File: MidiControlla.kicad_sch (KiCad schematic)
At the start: 4 parts, among them U1 TCRT5000, U2 TCRT5000, U3 TCRT5000, U4 TCRT5000

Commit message: Add espressif c3
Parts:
- added U5: ESP32-S3-DevKitC, Espressif:ESP32-S3-DevKitC, symbol Espressif:ESP32-S3-DevKitC
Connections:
- new net: U5.1 (3V3), U5.2 (3V3)
- new net: U5.22 (GND), U5.23 (GND), U5.24 (GND), U5.44 (GND)
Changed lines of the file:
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@@
+    )
+  )
+  (symbol (lib_id "Espressif:ESP32-S3-DevKitC") (at 64.77 95.25 0) (unit 1)
+    (in_bom yes) (on_board yes) (dnp no) (fields_autoplaced)
+    (property "Reference" "U5" (at 66.9641 140.97 0)
+      (effects (font (size 1.27 1.27)) (justify left))
+    )
+    (property "Value" "ESP32-S3-DevKitC" (at 66.9641 143.51 0)
+      (effects (font (size 1.27 1.27)) (justify left))
+    )
+    (property "Footprint" "Espressif:ESP32-S3-DevKitC" (at 64.77 152.4 0)
+      (effects (font (size 1.27 1.27)) hide)
+    )
+    (property "Datasheet" "" (at 5.08 97.79 0)
+      (effects (font (size 1.27 1.27)) hide)
+    )
+    (pin "41")
+    (pin "19")
+    (pin "40")
+    (pin "39")
+    (pin "14")
+    (pin "34")
+    (pin "35")
+    (pin "37")
+    (pin "38")
+    (pin "36")
+    (pin "4")
+    (pin "5")
+    (pin "22")
+    (pin "24")
+    (pin "25")
+    (pin "8")
+    (pin "9")
+    (pin "6")
+    (pin "7")
+    (pin "30")
+    (pin "26")
+    (pin "27")
+    (pin "29")
+    (pin "3")
+    (pin "23")
+    (pin "28")
+    (pin "42")
+    (pin "2")
+    (pin "10")
+    (pin "13")
+    (pin "15")
+    (pin "18")
+    (pin "20")
+    (pin "1")
+    (pin "43")
+    (pin "11")
+    (pin "12")
+    (pin "17")
+    (pin "44")
+    (pin "21")
+    (pin "16")
+    (pin "33")
+    (pin "32")
+    (pin "31")
+    (instances
+      (project "MidiControlla"
+        (path "/6c0d32a8-1440-498c-b764-68a3bc199eca"
+          (reference "U5") (unit 1)
+        )
+      )
     )
   )

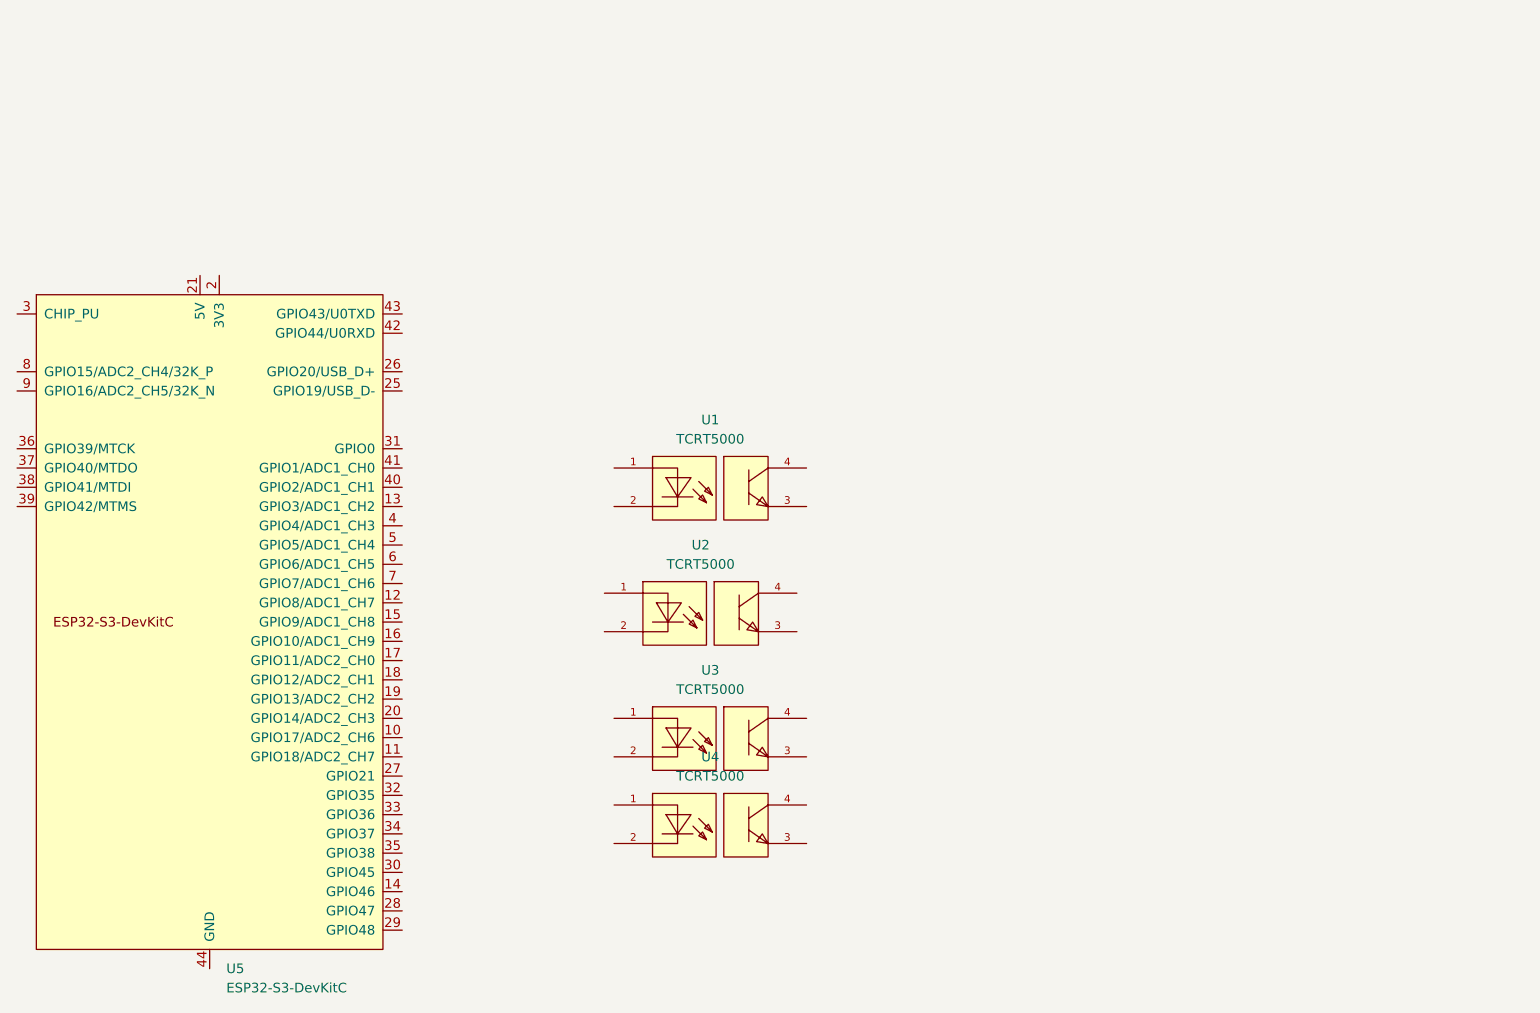
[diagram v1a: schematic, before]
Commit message: Add footprints
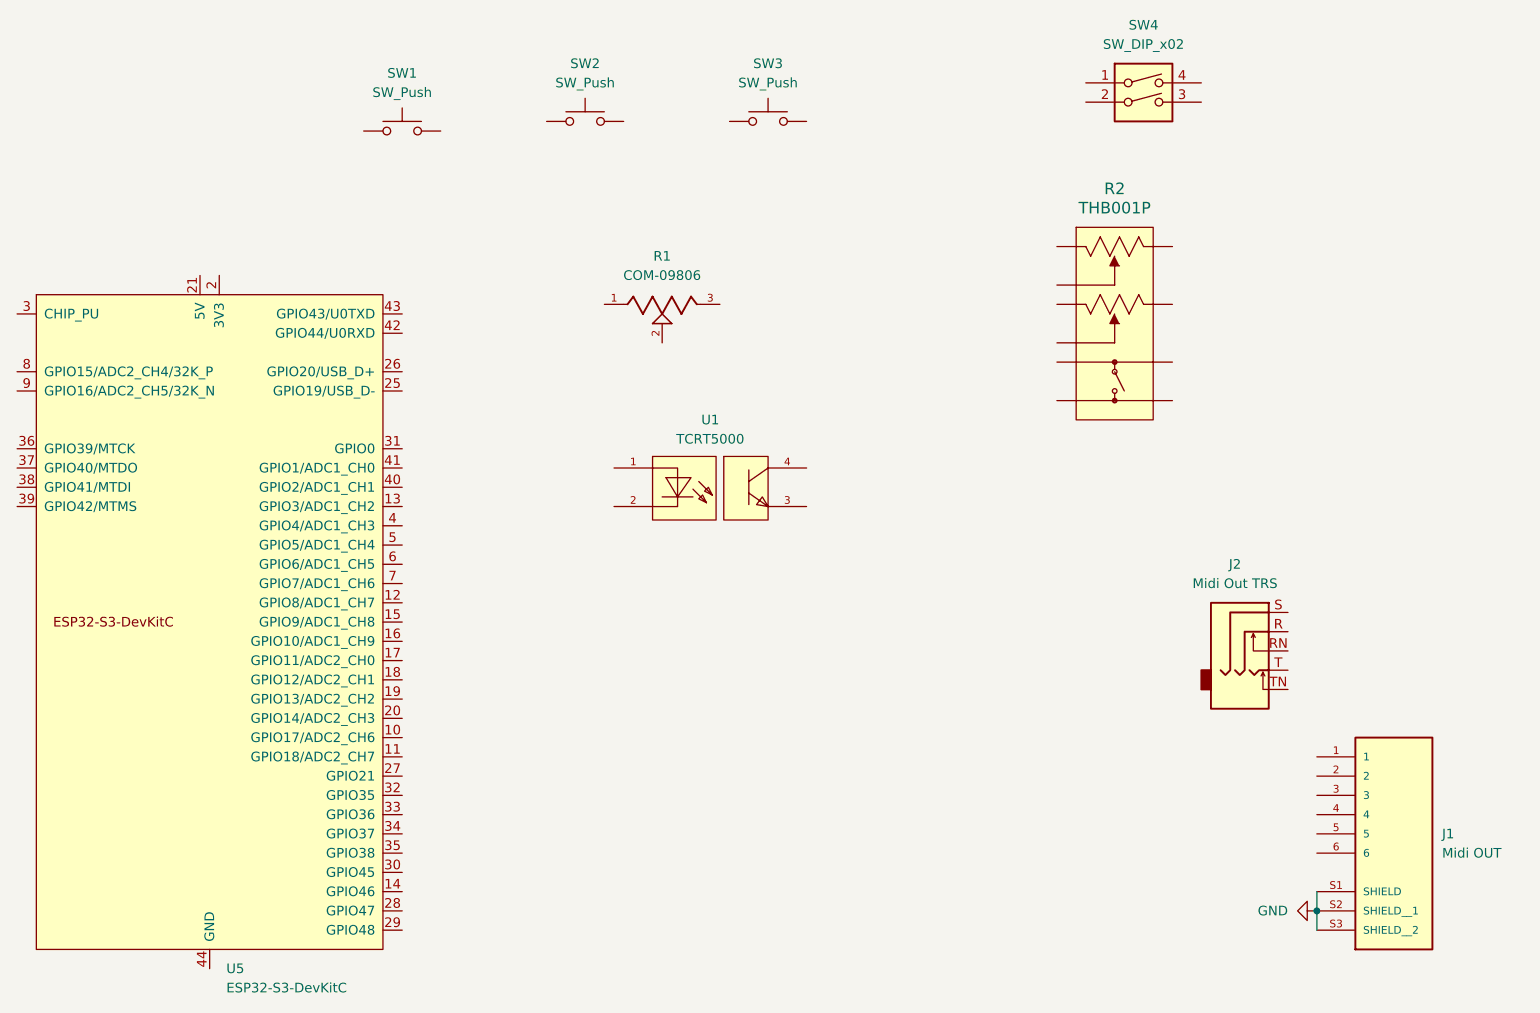
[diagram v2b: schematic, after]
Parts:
- removed U2, U3, U4: TCRT5000, jlc_footprints:OPTO-TH_TCRT5000, symbol jlc_symbols:TCRT5000
- added J1: Midi OUT, MD-60SM, symbol MD-60SM:MD-60SM
- added J2: Midi Out TRS, Connector_Audio:Jack_3.5mm_CUI_SJ2-3593D-SMT_Horizontal, symbol Connector_Audio:AudioJack3_SwitchTR
- added R1: COM-09806, COM-09806:COM-09806, symbol COM-09806:COM-09806
- added R2: THB001P, THB001P:THB001P, symbol THB001P:THB001P
- added SW1, SW2, SW3: SW_Push, pts636:pts636, symbol Switch:SW_Push
- added SW4: SW_DIP_x02, Button_Switch_THT:SW_DIP_SPSTx02_Slide_6.7x6.64mm_W7.62mm_P2.54mm_LowProfile, symbol Switch:SW_DIP_x02
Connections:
- new net GND: J1.S1 (SHIELD), J1.S2 (SHIELD__1), J1.S3 (SHIELD__2)
